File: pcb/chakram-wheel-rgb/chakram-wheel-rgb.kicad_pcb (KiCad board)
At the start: 2 copper layers, 13 x 10.1 mm, 4 parts, among them J1 Edge pins

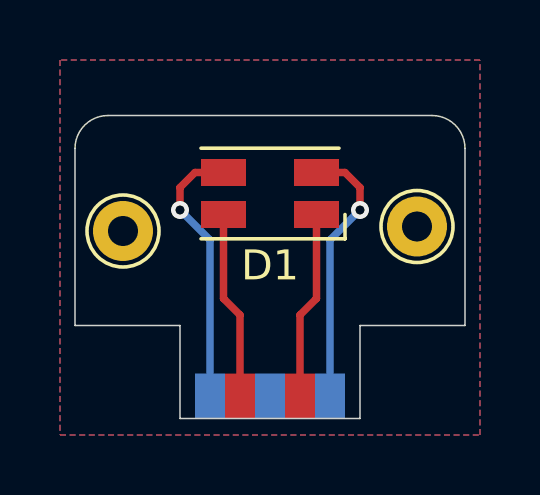
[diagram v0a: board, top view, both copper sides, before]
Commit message: Added generated schematics, updated silkscreen and RGB board shape
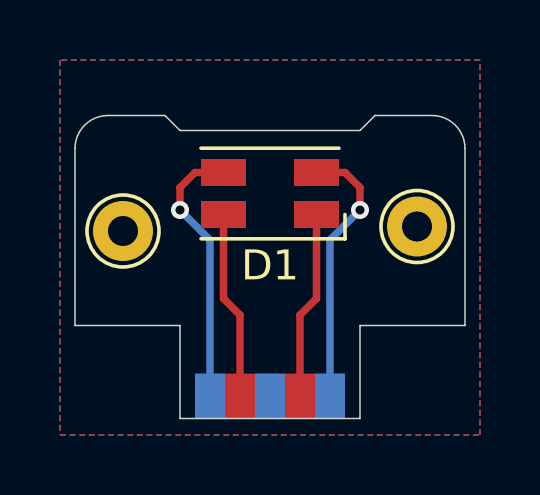
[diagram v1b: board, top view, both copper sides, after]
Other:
- outline, holes or cut-outs redrawn
- board text added: "moucha19"
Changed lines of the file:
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@@
 		(at 116.5 59.95 90)
 		(property "Reference" "J1"
-			(at 0 -4.2 -90)
-			(unlocked yes)
-			(layer "B.SilkS")
+			(at 1.65 0 0)
+			(unlocked yes)
+			(layer "F.SilkS")
+			(hide yes)
 			(effects
 				(font
@@
 					(thickness 0.1)
 				)
-				(justify mirror)
 			)
 		)
@@
 	)
 	(gr_line
+		(start 113.5 51.1)
+		(end 119.5 51.1)
+		(locked yes)
+		(stroke
+			(width 0.05)
+			(type default)
+		)
+		(layer "Edge.Cuts")
+	)
+	(gr_line
 		(start 110 57.6)
 		(end 113.5 57.6)
+		(locked yes)
+		(stroke
+			(width 0.05)
+			(type default)
+		)
+		(layer "Edge.Cuts")
+	)
+	(gr_line
+		(start 119.5 51.1)
+		(end 120 50.6)
 		(locked yes)
 		(stroke
@@
 	)
 	(gr_line
-		(start 111.1 50.6)
-		(end 121.9 50.6)
+		(start 113 50.6)
+		(end 113.5 51.1)
+		(locked yes)
+		(stroke
+			(width 0.05)
+			(type default)
+		)
+		(layer "Edge.Cuts")
+	)
+	(gr_line
+		(start 121.9 50.6)
+		(end 120 50.6)
 		(locked yes)
 		(stroke
@@
 		(start 113.5 60.7)
 		(end 119.5 60.7)
+		(locked yes)
+		(stroke
+			(width 0.05)
+			(type default)
+		)
+		(layer "Edge.Cuts")
+	)
+	(gr_line
+		(start 111.1 50.6)
+		(end 113 50.6)
 		(locked yes)
 		(stroke
@@
 	)
 	(gr_text "WHEEL RGB"
-		(at 116.5 52.25 0)
+		(at 116.5 52.3 0)
 		(layer "B.SilkS" knockout)
 		(effects
@@
 				(bold yes)
 			)
+			(justify mirror)
+		)
+	)
+	(gr_text "moucha19"
+		(at 116.5 56.5 0)
+		(layer "B.SilkS")
+		(effects
+			(font
+				(size 1 0.8)
+				(thickness 0.2)
+				(bold yes)
+			)
